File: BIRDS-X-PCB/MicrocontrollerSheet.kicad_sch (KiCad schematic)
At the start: 10 parts, among them J401 Conn_02x04_Odd_Even, J402 Conn_01x08, SW401 SW_Push, U401 STM32G031K8Tx, U402 MTT4B-Mini, U403 MT29F2G01ABAGDWB-IT-G_TR, Y401 ECS-2520SMV-080-FN-TR

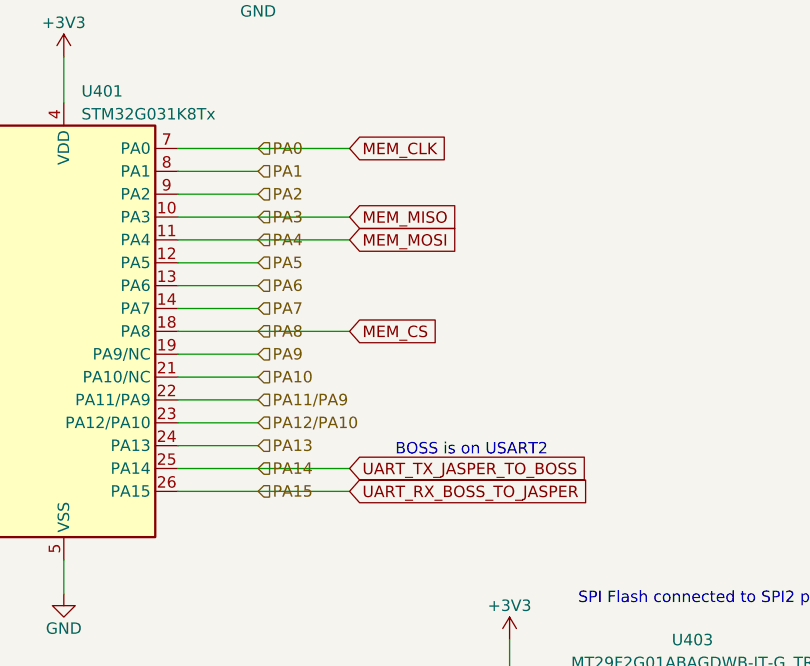
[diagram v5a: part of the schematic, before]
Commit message: Completed MCU & Experiment Circuit
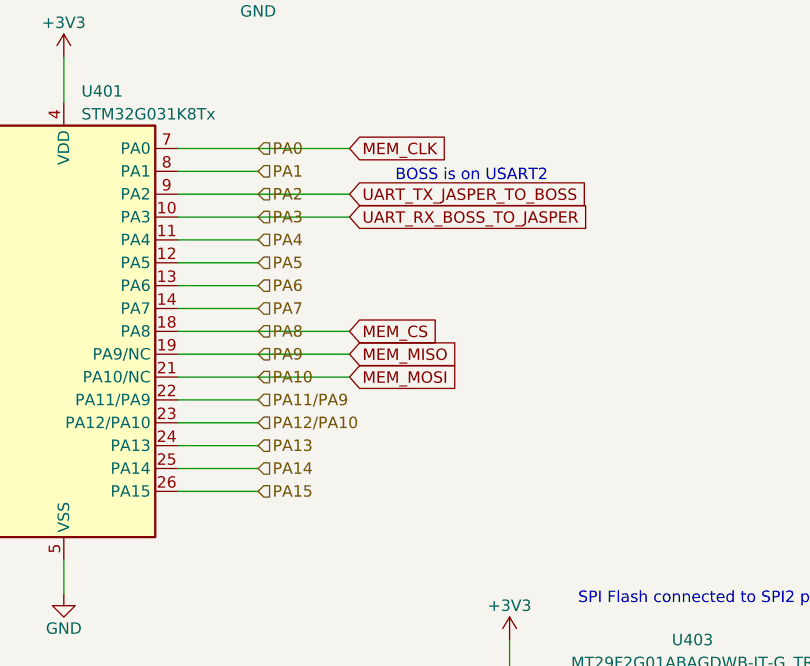
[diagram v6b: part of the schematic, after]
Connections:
- net PA10 is gone; now on net MEM_MOSI: U401.21 (PA10/NC)
- net PA2 is gone; now on net UART_TX_JASPER_TO_BOSS: U401.9 (PA2)
- net PA9 is gone; now on net MEM_MISO: U401.19 (PA9/NC)
- net MEM_MISO: no longer U401.10 (PA3)
- net MEM_MOSI: no longer U401.11 (PA4)
- net UART_RX_BOSS_TO_JASPER: now also U401.10 (PA3); no longer U401.26 (PA15)
- net UART_TX_JASPER_TO_BOSS: no longer U401.25 (PA14)
- new net PA14: U401.25 (PA14)
- new net PA15: U401.26 (PA15)
- new net PA4: U401.11 (PA4)
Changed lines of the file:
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@@
+    (stroke (width 0) (type default))
+  )
+  (wire (pts (xy 153.67 74.93) (xy 172.72 74.93))
     (stroke (width 0) (type default))
   )
@@
     (stroke (width 0) (type default))
   )
+  (wire (pts (xy 153.67 113.03) (xy 162.56 113.03))
+    (stroke (width 0) (type default))
+  )
   (wire (pts (xy 82.55 82.55) (xy 125.73 82.55))
     (stroke (width 0) (type default))
@@
     (stroke (width 0) (type default))
   )
+  (wire (pts (xy 153.67 110.49) (xy 162.56 110.49))
+    (stroke (width 0) (type default))
+  )
   (wire (pts (xy 36.83 81.28) (xy 36.83 82.55))
     (stroke (width 0) (type default))
@@
     (stroke (width 0) (type default))
   )
-  (wire (pts (xy 153.67 80.01) (xy 162.56 80.01))
-    (stroke (width 0) (type default))
-  )
   (wire (pts (xy 124.46 107.95) (xy 124.46 154.94))
     (stroke (width 0) (type default))
@@
     (stroke (width 0) (type default))
   )
-  (wire (pts (xy 153.67 85.09) (xy 172.72 85.09))
-    (stroke (width 0) (type default))
-  )
   (wire (pts (xy 187.96 143.51) (xy 198.12 143.51))
     (stroke (width 0) (type default))
@@
     (stroke (width 0) (type default))
   )
+  (wire (pts (xy 153.67 97.79) (xy 172.72 97.79))
+    (stroke (width 0) (type default))
+  )
   (wire (pts (xy 198.12 138.43) (xy 193.04 138.43))
     (stroke (width 0) (type default))
@@
     (stroke (width 0) (type default))
   )
-  (wire (pts (xy 153.67 74.93) (xy 172.72 74.93))
-    (stroke (width 0) (type default))
-  )
   (wire (pts (xy 153.67 92.71) (xy 162.56 92.71))
     (stroke (width 0) (type default))
@@
     (stroke (width 0) (type default))
   )
+  (wire (pts (xy 153.67 100.33) (xy 172.72 100.33))
+    (stroke (width 0) (type default))
+  )
   (wire (pts (xy 120.65 74.93) (xy 120.65 58.42))
     (stroke (width 0) (type default))
@@
     (stroke (width 0) (type default))
   )
-  (wire (pts (xy 153.67 100.33) (xy 162.56 100.33))
+  (wire (pts (xy 153.67 85.09) (xy 162.56 85.09))
     (stroke (width 0) (type default))
   )
@@
     (stroke (width 0) (type default))
   )
+  (wire (pts (xy 116.84 102.87) (xy 125.73 102.87))
+    (stroke (width 0) (type default))
+  )
+  (wire (pts (xy 153.67 82.55) (xy 172.72 82.55))
+    (stroke (width 0) (type default))
+  )
+  (wire (pts (xy 114.3 147.32) (xy 119.38 147.32))
+    (stroke (width 0) (type default))
+  )
+  (wire (pts (xy 101.6 154.94) (xy 114.3 154.94))
+    (stroke (width 0) (type default))
+  )
+  (wire (pts (xy 121.92 149.86) (xy 128.27 149.86))
+    (stroke (width 0) (type default))
+  )
+  (wire (pts (xy 140.97 64.77) (xy 140.97 69.85))
+    (stroke (width 0) (type default))
+  )
+  (wire (pts (xy 193.04 138.43) (xy 193.04 151.13))
+    (stroke (width 0) (type default))
+  )
+  (wire (pts (xy 195.58 149.86) (xy 231.14 149.86))
+    (stroke (width 0) (type default))
+  )
+  (wire (pts (xy 195.58 140.97) (xy 195.58 149.86))
+    (stroke (width 0) (type default))
+  )
+  (wire (pts (xy 153.67 80.01) (xy 172.72 80.01))
+    (stroke (width 0) (type default))
+  )
+  (wire (pts (xy 157.48 52.07) (xy 162.56 52.07))
+    (stroke (width 0) (type default))
+  )
+  (wire (pts (xy 193.04 151.13) (xy 240.03 151.13))
+    (stroke (width 0) (type default))
+  )
+  (wire (pts (xy 116.84 142.24) (xy 116.84 152.4))
+    (stroke (width 0) (type default))
+  )
+  (wire (pts (xy 96.52 71.12) (xy 96.52 69.85))
+    (stroke (width 0) (type default))
+  )
+  (wire (pts (xy 153.67 90.17) (xy 162.56 90.17))
+    (stroke (width 0) (type default))
+  )
+  (wire (pts (xy 101.6 147.32) (xy 114.3 147.32))
+    (stroke (width 0) (type default))
+  )
   (wire (pts (xy 153.67 95.25) (xy 172.72 95.25))
     (stroke (width 0) (type default))
   )
-  (wire (pts (xy 153.67 113.03) (xy 172.72 113.03))
-    (stroke (width 0) (type default))
-  )
-  (wire (pts (xy 116.84 102.87) (xy 125.73 102.87))
-    (stroke (width 0) (type default))
-  )
-  (wire (pts (xy 114.3 147.32) (xy 119.38 147.32))
-    (stroke (width 0) (type default))
-  )
-  (wire (pts (xy 101.6 154.94) (xy 114.3 154.94))
-    (stroke (width 0) (type default))
-  )
-  (wire (pts (xy 121.92 149.86) (xy 128.27 149.86))
-    (stroke (width 0) (type default))
-  )
-  (wire (pts (xy 140.97 64.77) (xy 140.97 69.85))
-    (stroke (width 0) (type default))
-  )
-  (wire (pts (xy 193.04 138.43) (xy 193.04 151.13))
-    (stroke (width 0) (type default))
-  )
-  (wire (pts (xy 153.67 82.55) (xy 172.72 82.55))
-    (stroke (width 0) (type default))
-  )
-  (wire (pts (xy 195.58 149.86) (xy 231.14 149.86))
-    (stroke (width 0) (type default))
-  )
-  (wire (pts (xy 195.58 140.97) (xy 195.58 149.86))
-    (stroke (width 0) (type default))
-  )
-  (wire (pts (xy 157.48 52.07) (xy 162.56 52.07))
-    (stroke (width 0) (type default))
-  )
-  (wire (pts (xy 193.04 151.13) (xy 240.03 151.13))
-    (stroke (width 0) (type default))
-  )
-  (wire (pts (xy 116.84 142.24) (xy 116.84 152.4))
-    (stroke (width 0) (type default))
-  )
-  (wire (pts (xy 96.52 71.12) (xy 96.52 69.85))
-    (stroke (width 0) (type default))
-  )
-  (wire (pts (xy 153.67 90.17) (xy 162.56 90.17))
-    (stroke (width 0) (type default))
-  )
-  (wire (pts (xy 101.6 147.32) (xy 114.3 147.32))
-    (stroke (width 0) (type default))
-  )
-  (wire (pts (xy 153.67 110.49) (xy 172.72 110.49))
-    (stroke (width 0) (type default))
-  )
   (wire (pts (xy 116.84 97.79) (xy 125.73 97.79))
     (stroke (width 0) (type default))
@@
   )
   (wire (pts (xy 198.12 140.97) (xy 195.58 140.97))
-    (stroke (width 0) (type default))
-  )
-  (wire (pts (xy 153.67 97.79) (xy 162.56 97.79))
     (stroke (width 0) (type default))
   )
@@
     (effects (font (size 1.27 1.27)) (justify left bottom))
   )
-  (text "BOSS is on USART2" (at 177.8 109.22 0)
+  (text "BOSS is on USART2" (at 177.8 78.74 0)
     (effects (font (size 1.27 1.27)) (justify left bottom))
   )
@@
     )
   )
-  (global_label "UART_RX_BOSS_TO_JASPER" (shape input) (at 172.72 113.03 0) (fields_autoplaced)
-    (effects (font (size 1.27 1.27)) (justify left))
-    (property "Intersheetrefs" "${INTERSHEET_REFS}" (at 200.9047 113.03 0)
+  (global_label "UART_RX_BOSS_TO_JASPER" (shape input) (at 172.72 82.55 0) (fields_autoplaced)
+    (effects (font (size 1.27 1.27)) (justify left))
+    (property "Intersheetrefs" "${INTERSHEET_REFS}" (at 200.9047 82.55 0)
       (effects (font (size 1.27 1.27)) (justify left) hide)
     )
@@
     )
   )
-  (global_label "MEM_MISO" (shape input) (at 172.72 82.55 0) (fields_autoplaced)
-    (effects (font (size 1.27 1.27)) (justify left))
-    (property "Intersheetrefs" "${INTERSHEET_REFS}" (at 185.2414 82.55 0)
+  (global_label "MEM_MISO" (shape input) (at 172.72 97.79 0) (fields_autoplaced)
+    (effects (font (size 1.27 1.27)) (justify left))
+    (property "Intersheetrefs" "${INTERSHEET_REFS}" (at 185.2414 97.79 0)
       (effects (font (size 1.27 1.27)) (justify left) hide)
     )
@@
     )
   )
-  (global_label "MEM_MOSI" (shape input) (at 172.72 85.09 0) (fields_autoplaced)
-    (effects (font (size 1.27 1.27)) (justify left))
-    (property "Intersheetrefs" "${INTERSHEET_REFS}" (at 185.2414 85.09 0)
+  (global_label "MEM_MOSI" (shape input) (at 172.72 100.33 0) (fields_autoplaced)
+    (effects (font (size 1.27 1.27)) (justify left))
+    (property "Intersheetrefs" "${INTERSHEET_REFS}" (at 185.2414 100.33 0)
       (effects (font (size 1.27 1.27)) (justify left) hide)
     )
@@
     )
   )
-  (global_label "UART_TX_JASPER_TO_BOSS" (shape input) (at 172.72 110.49 0) (fields_autoplaced)
-    (effects (font (size 1.27 1.27)) (justify left))
-    (property "Intersheetrefs" "${INTERSHEET_REFS}" (at 200.6023 110.49 0)
-      (effects (font (size 1.27 1.27)) (justify left) hide)
-    )
+  (global_label "UART_TX_JASPER_TO_BOSS" (shape input) (at 172.72 80.01 0) (fields_autoplaced)
+    (effects (font (size 1.27 1.27)) (justify left))
+    (property "Intersheetrefs" "${INTERSHEET_REFS}" (at 200.6023 80.01 0)
+      (effects (font (size 1.27 1.27)) (justify left) hide)
+    )
